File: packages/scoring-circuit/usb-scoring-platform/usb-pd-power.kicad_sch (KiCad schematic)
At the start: 33 parts, among them J12 PD service: GND SDA SCL, Q4 BSS138, Q5 BSS138, U19 LMR36510ADDAR, U20 TPS259470LRPWR, U5 STUSB4500QTR, U6 REC30K-2405SZ

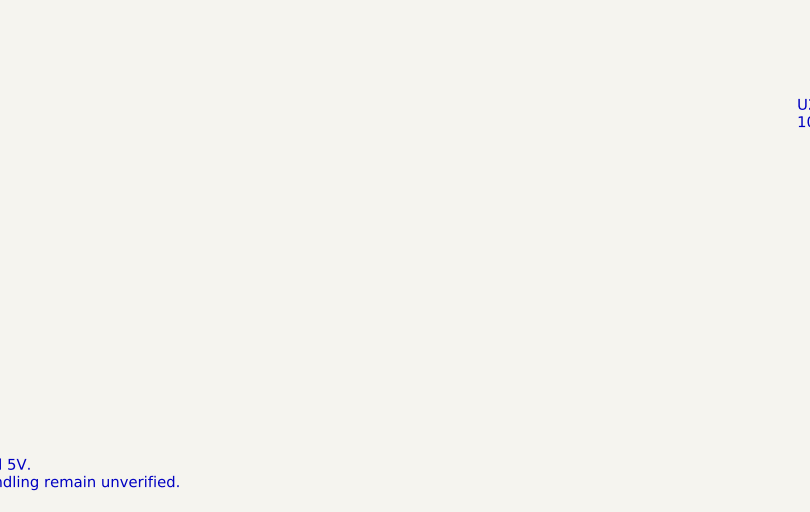
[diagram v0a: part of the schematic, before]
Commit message: feat(scoring-circuit): route protected isolated-power feed and eFuse support
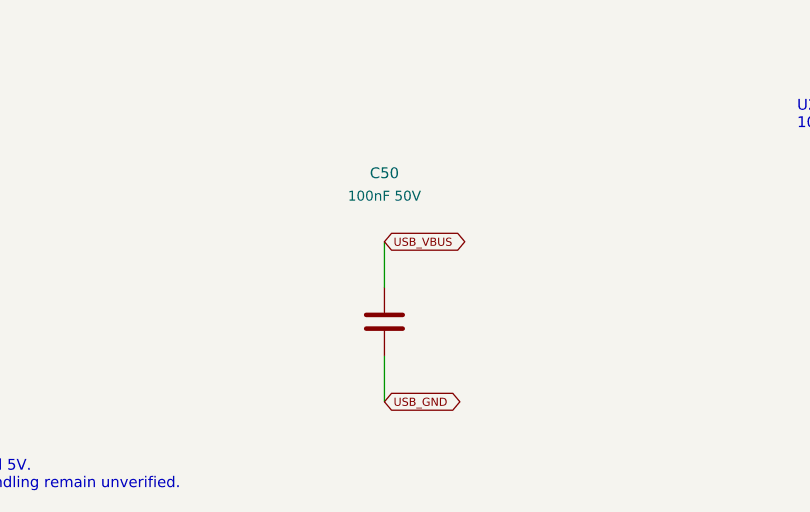
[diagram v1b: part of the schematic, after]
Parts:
- added C50: 100nF 50V, Capacitor_SMD:C_0805_2012Metric, symbol Device:C
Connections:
- net USB_GND: now also C50.2
- net USB_VBUS: now also C50.1
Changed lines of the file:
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@@
 (global_label "GND" (shape bidirectional) (at 519.43 373.38 0) (effects (font (size .9 .9)) (justify left)) (property "Intersheetrefs" "" (at 519.43 373.38 0) (effects (font (size 1 1)) (hide yes))))
 (symbol (lib_id "Device:C") (at 519.43 364.49 0) (unit 1) (in_bom yes) (on_board yes) (dnp no) (property "Reference" "C49" (at 519.43 347.98 0) (effects (font (size 1.2 1.2)))) (property "Value" "10uF 16V X7R" (at 519.43 350.52 0) (effects (font (size 1.1 1.1)))) (property "Footprint" "Capacitor_SMD:C_1206_3216Metric" (at 519.43 364.49 0) (effects (font (size 1 1)) (hide yes))) (property "Datasheet" "" (at 519.43 364.49 0) (effects (font (size 1 1)) (hide yes))) (instances (project "usb-scoring-platform" (path "/20cc8167-128c-446a-a106-f942323e143f/972b77fe-bd38-49a7-88fc-3c741d64cdb1" (reference "C49") (unit 1)))) (pin "1") (pin "2"))
+(wire (pts (xy 184.15 365.76) (xy 184.15 360.68)) (stroke (width 0) (type default)))
+(global_label "USB_VBUS" (shape bidirectional) (at 184.15 360.68 0) (effects (font (size .9 .9)) (justify left)) (property "Intersheetrefs" "" (at 184.15 360.68 0) (effects (font (size 1 1)) (hide yes))))
+(wire (pts (xy 184.15 373.38) (xy 184.15 378.46)) (stroke (width 0) (type default)))
+(global_label "USB_GND" (shape bidirectional) (at 184.15 378.46 0) (effects (font (size .9 .9)) (justify left)) (property "Intersheetrefs" "" (at 184.15 378.46 0) (effects (font (size 1 1)) (hide yes))))
+(symbol (lib_id "Device:C") (at 184.15 369.57 0) (unit 1) (in_bom yes) (on_board yes) (dnp no) (property "Reference" "C50" (at 184.15 353.06 0) (effects (font (size 1.2 1.2)))) (property "Value" "100nF 50V" (at 184.15 355.6 0) (effects (font (size 1.1 1.1)))) (property "Footprint" "Capacitor_SMD:C_0805_2012Metric" (at 184.15 369.57 0) (effects (font (size 1 1)) (hide yes))) (property "Datasheet" "" (at 184.15 369.57 0) (effects (font (size 1 1)) (hide yes))) (instances (project "usb-scoring-platform" (path "/20cc8167-128c-446a-a106-f942323e143f/972b77fe-bd38-49a7-88fc-3c741d64cdb1" (reference "C50") (unit 1)))) (pin "1") (pin "2"))
 (text "ONE USB-C: J1 VBUS / CC / USB_GND feed this primary-side sheet; D+/D- go through U18." (at 20 18 0) (effects (font (size 2 2)) (justify left top)))
 (text "No primary USB_GND connection to board GND. Only U18 and U6 cross the isolation boundary. Prototype: not for fabrication or fencer use." (at 20 27 0) (effects (font (size 1.2 1.2)) (justify left top)))

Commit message: feat(scoring-circuit): select exact prototype resistor parts
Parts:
- R88, R89: MPN (none) -> RC2512FK-071KL; Manufacturer (none) -> YAGEO
- R90, R92, R93: MPN (none) -> RC0603FR-07100KL; Manufacturer (none) -> YAGEO
- R91: MPN (none) -> RC0603FR-0724K9L; Manufacturer (none) -> YAGEO
- R94: MPN (none) -> RT0603BRD07140KL; Manufacturer (none) -> YAGEO
- R95, R97: MPN (none) -> RT0603BRD0710KL; Manufacturer (none) -> YAGEO
- R96: MPN (none) -> RT0603BRD07172KL; Manufacturer (none) -> YAGEO
- R98: MPN (none) -> RC0603FR-071K37L; Manufacturer (none) -> YAGEO

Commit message: feat(scoring-circuit): select bypass and timing capacitors
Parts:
- C42, C48: MPN (none) -> C1608X7R1H104K080AA; Manufacturer (none) -> TDK
- C45: MPN (none) -> C1608X7R1H103K080AA; Manufacturer (none) -> TDK
- C46, C50: MPN (none) -> C2012X7R2A104K125AA; Manufacturer (none) -> TDK

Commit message: feat(scoring-circuit): select local supply capacitors
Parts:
- C37, C38, C41: MPN (none) -> C1608X7R1H105K080AB; Manufacturer (none) -> TDK
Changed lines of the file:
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@@
 (wire (pts (xy 80.01 153.67) (xy 80.01 158.75)) (stroke (width 0) (type default)))
 (global_label "USB_GND" (shape bidirectional) (at 80.01 158.75 0) (effects (font (size .9 .9)) (justify left)) (property "Intersheetrefs" "" (at 80.01 158.75 0) (effects (font (size 1 1)) (hide yes))))
-(symbol (lib_id "Device:C") (at 80.01 149.86 0) (unit 1) (in_bom yes) (on_board yes) (dnp no) (property "Reference" "C37" (at 80.01 133.35000000000002 0) (effects (font (size 1.2 1.2)))) (property "Value" "1uF 10V" (at 80.01 135.89000000000001 0) (effects (font (size 1.1 1.1)))) (property "Footprint" "Capacitor_SMD:C_0603_1608Metric" (at 80.01 149.86 0) (effects (font (size 1 1)) (hide yes))) (property "Datasheet" "" (at 80.01 149.86 0) (effects (font (size 1 1)) (hide yes))) (instances (project "usb-scoring-platform" (path "/20cc8167-128c-446a-a106-f942323e143f/972b77fe-bd38-49a7-88fc-3c741d64cdb1" (reference "C37") (unit 1)))) (pin "1") (pin "2"))
+(symbol (lib_id "Device:C") (at 80.01 149.86 0) (unit 1) (in_bom yes) (on_board yes) (dnp no) (property "Reference" "C37" (at 80.01 133.35000000000002 0) (effects (font (size 1.2 1.2)))) (property "Value" "1uF 10V" (at 80.01 135.89000000000001 0) (effects (font (size 1.1 1.1)))) (property "Footprint" "Capacitor_SMD:C_0603_1608Metric" (at 80.01 149.86 0) (effects (font (size 1 1)) (hide yes))) (property "Manufacturer" "TDK" (at 80.01 149.86 0) (effects (font (size 1 1)) (hide yes))) (property "MPN" "C1608X7R1H105K080AB" (at 80.01 149.86 0) (effects (font (size 1 1)) (hide yes))) (property "Datasheet" "https://product.tdk.com/en/search/capacitor/ceramic/mlcc/info?part_no=C1608X7R1H105K080AB" (at 80.01 149.86 0) (effects (font (size 1 1)) (hide yes))) (instances (project "usb-scoring-platform" (path "/20cc8167-128c-446a-a106-f942323e143f/972b77fe-bd38-49a7-88fc-3c741d64cdb1" (reference "C37") (unit 1)))) (pin "1") (pin "2"))
 (wire (pts (xy 119.38 146.05) (xy 119.38 140.97)) (stroke (width 0) (type default)))
 (global_label "PD_VREG2V7" (shape bidirectional) (at 119.38 140.97 0) (effects (font (size .9 .9)) (justify left)) (property "Intersheetrefs" "" (at 119.38 140.97 0) (effects (font (size 1 1)) (hide yes))))
 (wire (pts (xy 119.38 153.67) (xy 119.38 158.75)) (stroke (width 0) (type default)))
 (global_label "USB_GND" (shape bidirectional) (at 119.38 158.75 0) (effects (font (size .9 .9)) (justify left)) (property "Intersheetrefs" "" (at 119.38 158.75 0) (effects (font (size 1 1)) (hide yes))))
-(symbol (lib_id "Device:C") (at 119.38 149.86 0) (unit 1) (in_bom yes) (on_board yes) (dnp no) (property "Reference" "C38" (at 119.38 133.35000000000002 0) (effects (font (size 1.2 1.2)))) (property "Value" "1uF 10V" (at 119.38 135.89000000000001 0) (effects (font (size 1.1 1.1)))) (property "Footprint" "Capacitor_SMD:C_0603_1608Metric" (at 119.38 149.86 0) (effects (font (size 1 1)) (hide yes))) (property "Datasheet" "" (at 119.38 149.86 0) (effects (font (size 1 1)) (hide yes))) (instances (project "usb-scoring-platform" (path "/20cc8167-128c-446a-a106-f942323e143f/972b77fe-bd38-49a7-88fc-3c741d64cdb1" (reference "C38") (unit 1)))) (pin "1") (pin "2"))
+(symbol (lib_id "Device:C") (at 119.38 149.86 0) (unit 1) (in_bom yes) (on_board yes) (dnp no) (property "Reference" "C38" (at 119.38 133.35000000000002 0) (effects (font (size 1.2 1.2)))) (property "Value" "1uF 10V" (at 119.38 135.89000000000001 0) (effects (font (size 1.1 1.1)))) (property "Footprint" "Capacitor_SMD:C_0603_1608Metric" (at 119.38 149.86 0) (effects (font (size 1 1)) (hide yes))) (property "Manufacturer" "TDK" (at 119.38 149.86 0) (effects (font (size 1 1)) (hide yes))) (property "MPN" "C1608X7R1H105K080AB" (at 119.38 149.86 0) (effects (font (size 1 1)) (hide yes))) (property "Datasheet" "https://product.tdk.com/en/search/capacitor/ceramic/mlcc/info?part_no=C1608X7R1H105K080AB" (at 119.38 149.86 0) (effects (font (size 1 1)) (hide yes))) (instances (project "usb-scoring-platform" (path "/20cc8167-128c-446a-a106-f942323e143f/972b77fe-bd38-49a7-88fc-3c741d64cdb1" (reference "C38") (unit 1)))) (pin "1") (pin "2"))
 (wire (pts (xy 160.02 146.05) (xy 160.02 140.97)) (stroke (width 0) (type default)))
 (global_label "USB_VBUS" (shape bidirectional) (at 160.02 140.97 0) (effects (font (size .9 .9)) (justify left)) (property "Intersheetrefs" "" (at 160.02 140.97 0) (effects (font (size 1 1)) (hide yes))))
@@
 (wire (pts (xy 325.12 153.67) (xy 325.12 158.75)) (stroke (width 0) (type default)))
 (global_label "USB_GND" (shape bidirectional) (at 325.12 158.75 0) (effects (font (size .9 .9)) (justify left)) (property "Intersheetrefs" "" (at 325.12 158.75 0) (effects (font (size 1 1)) (hide yes))))
-(symbol (lib_id "Device:C") (at 325.12 149.86 0) (unit 1) (in_bom yes) (on_board yes) (dnp no) (property "Reference" "C41" (at 325.12 133.35000000000002 0) (effects (font (size 1.2 1.2)))) (property "Value" "1uF 10V" (at 325.12 135.89000000000001 0) (effects (font (size 1.1 1.1)))) (property "Footprint" "Capacitor_SMD:C_0603_1608Metric" (at 325.12 149.86 0) (effects (font (size 1 1)) (hide yes))) (property "Datasheet" "" (at 325.12 149.86 0) (effects (font (size 1 1)) (hide yes))) (instances (project "usb-scoring-platform" (path "/20cc8167-128c-446a-a106-f942323e143f/972b77fe-bd38-49a7-88fc-3c741d64cdb1" (reference "C41") (unit 1)))) (pin "1") (pin "2"))
+(symbol (lib_id "Device:C") (at 325.12 149.86 0) (unit 1) (in_bom yes) (on_board yes) (dnp no) (property "Reference" "C41" (at 325.12 133.35000000000002 0) (effects (font (size 1.2 1.2)))) (property "Value" "1uF 10V" (at 325.12 135.89000000000001 0) (effects (font (size 1.1 1.1)))) (property "Footprint" "Capacitor_SMD:C_0603_1608Metric" (at 325.12 149.86 0) (effects (font (size 1 1)) (hide yes))) (property "Manufacturer" "TDK" (at 325.12 149.86 0) (effects (font (size 1 1)) (hide yes))) (property "MPN" "C1608X7R1H105K080AB" (at 325.12 149.86 0) (effects (font (size 1 1)) (hide yes))) (property "Datasheet" "https://product.tdk.com/en/search/capacitor/ceramic/mlcc/info?part_no=C1608X7R1H105K080AB" (at 325.12 149.86 0) (effects (font (size 1 1)) (hide yes))) (instances (project "usb-scoring-platform" (path "/20cc8167-128c-446a-a106-f942323e143f/972b77fe-bd38-49a7-88fc-3c741d64cdb1" (reference "C41") (unit 1)))) (pin "1") (pin "2"))
 (wire (pts (xy 364.49 146.05) (xy 364.49 140.97)) (stroke (width 0) (type default)))
 (global_label "USB_BUCK_BOOT" (shape bidirectional) (at 364.49 140.97 0) (effects (font (size .9 .9)) (justify left)) (property "Intersheetrefs" "" (at 364.49 140.97 0) (effects (font (size 1 1)) (hide yes))))

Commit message: feat(scoring-circuit): select USB input capacitors
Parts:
- C36: MPN (none) -> C2012X7R1H105K125AB; Manufacturer (none) -> TDK
- C39: MPN (none) -> C3216X7R1H225K160AB; Manufacturer (none) -> TDK
- C40: MPN (none) -> C2012X7R1H224K125AA; Manufacturer (none) -> TDK
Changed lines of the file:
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@@
 (wire (pts (xy 39.37 153.67) (xy 39.37 158.75)) (stroke (width 0) (type default)))
 (global_label "USB_GND" (shape bidirectional) (at 39.37 158.75 0) (effects (font (size .9 .9)) (justify left)) (property "Intersheetrefs" "" (at 39.37 158.75 0) (effects (font (size 1 1)) (hide yes))))
-(symbol (lib_id "Device:C") (at 39.37 149.86 0) (unit 1) (in_bom yes) (on_board yes) (dnp no) (property "Reference" "C36" (at 39.37 133.35000000000002 0) (effects (font (size 1.2 1.2)))) (property "Value" "1uF 50V" (at 39.37 135.89000000000001 0) (effects (font (size 1.1 1.1)))) (property "Footprint" "Capacitor_SMD:C_0805_2012Metric" (at 39.37 149.86 0) (effects (font (size 1 1)) (hide yes))) (property "Datasheet" "" (at 39.37 149.86 0) (effects (font (size 1 1)) (hide yes))) (instances (project "usb-scoring-platform" (path "/20cc8167-128c-446a-a106-f942323e143f/972b77fe-bd38-49a7-88fc-3c741d64cdb1" (reference "C36") (unit 1)))) (pin "1") (pin "2"))
+(symbol (lib_id "Device:C") (at 39.37 149.86 0) (unit 1) (in_bom yes) (on_board yes) (dnp no) (property "Reference" "C36" (at 39.37 133.35000000000002 0) (effects (font (size 1.2 1.2)))) (property "Value" "1uF 50V" (at 39.37 135.89000000000001 0) (effects (font (size 1.1 1.1)))) (property "Footprint" "Capacitor_SMD:C_0805_2012Metric" (at 39.37 149.86 0) (effects (font (size 1 1)) (hide yes))) (property "Datasheet" "https://product.tdk.com/en/search/capacitor/ceramic/mlcc/info?part_no=C2012X7R1H105K125AB" (at 39.37 149.86 0) (effects (font (size 1 1)) (hide yes))) (property "Manufacturer" "TDK" (at 0 0 0) (effects (font (size 1 1)) (hide yes))) (property "MPN" "C2012X7R1H105K125AB" (at 0 0 0) (effects (font (size 1 1)) (hide yes))) (instances (project "usb-scoring-platform" (path "/20cc8167-128c-446a-a106-f942323e143f/972b77fe-bd38-49a7-88fc-3c741d64cdb1" (reference "C36") (unit 1)))) (pin "1") (pin "2"))
 (wire (pts (xy 80.01 146.05) (xy 80.01 140.97)) (stroke (width 0) (type default)))
 (global_label "PD_VREG1V2" (shape bidirectional) (at 80.01 140.97 0) (effects (font (size .9 .9)) (justify left)) (property "Intersheetrefs" "" (at 80.01 140.97 0) (effects (font (size 1 1)) (hide yes))))
@@
 (wire (pts (xy 245.11 153.67) (xy 245.11 158.75)) (stroke (width 0) (type default)))
 (global_label "USB_GND" (shape bidirectional) (at 245.11 158.75 0) (effects (font (size .9 .9)) (justify left)) (property "Intersheetrefs" "" (at 245.11 158.75 0) (effects (font (size 1 1)) (hide yes))))
-(symbol (lib_id "Device:C") (at 245.11 149.86 0) (unit 1) (in_bom yes) (on_board yes) (dnp no) (property "Reference" "C39" (at 245.11 133.35000000000002 0) (effects (font (size 1.2 1.2)))) (property "Value" "2.2uF 50V" (at 245.11 135.89000000000001 0) (effects (font (size 1.1 1.1)))) (property "Footprint" "Capacitor_SMD:C_1206_3216Metric" (at 245.11 149.86 0) (effects (font (size 1 1)) (hide yes))) (property "Datasheet" "" (at 245.11 149.86 0) (effects (font (size 1 1)) (hide yes))) (instances (project "usb-scoring-platform" (path "/20cc8167-128c-446a-a106-f942323e143f/972b77fe-bd38-49a7-88fc-3c741d64cdb1" (reference "C39") (unit 1)))) (pin "1") (pin "2"))
+(symbol (lib_id "Device:C") (at 245.11 149.86 0) (unit 1) (in_bom yes) (on_board yes) (dnp no) (property "Reference" "C39" (at 245.11 133.35000000000002 0) (effects (font (size 1.2 1.2)))) (property "Value" "2.2uF 50V" (at 245.11 135.89000000000001 0) (effects (font (size 1.1 1.1)))) (property "Footprint" "Capacitor_SMD:C_1206_3216Metric" (at 245.11 149.86 0) (effects (font (size 1 1)) (hide yes))) (property "Datasheet" "https://product.tdk.com/en/search/capacitor/ceramic/mlcc/info?part_no=C3216X7R1H225K160AB" (at 245.11 149.86 0) (effects (font (size 1 1)) (hide yes))) (property "Manufacturer" "TDK" (at 0 0 0) (effects (font (size 1 1)) (hide yes))) (property "MPN" "C3216X7R1H225K160AB" (at 0 0 0) (effects (font (size 1 1)) (hide yes))) (instances (project "usb-scoring-platform" (path "/20cc8167-128c-446a-a106-f942323e143f/972b77fe-bd38-49a7-88fc-3c741d64cdb1" (reference "C39") (unit 1)))) (pin "1") (pin "2"))
 (wire (pts (xy 284.48 146.05) (xy 284.48 140.97)) (stroke (width 0) (type default)))
 (global_label "USB_VBUS" (shape bidirectional) (at 284.48 140.97 0) (effects (font (size .9 .9)) (justify left)) (property "Intersheetrefs" "" (at 284.48 140.97 0) (effects (font (size 1 1)) (hide yes))))
 (wire (pts (xy 284.48 153.67) (xy 284.48 158.75)) (stroke (width 0) (type default)))
 (global_label "USB_GND" (shape bidirectional) (at 284.48 158.75 0) (effects (font (size .9 .9)) (justify left)) (property "Intersheetrefs" "" (at 284.48 158.75 0) (effects (font (size 1 1)) (hide yes))))
-(symbol (lib_id "Device:C") (at 284.48 149.86 0) (unit 1) (in_bom yes) (on_board yes) (dnp no) (property "Reference" "C40" (at 284.48 133.35000000000002 0) (effects (font (size 1.2 1.2)))) (property "Value" "220nF 50V" (at 284.48 135.89000000000001 0) (effects (font (size 1.1 1.1)))) (property "Footprint" "Capacitor_SMD:C_0805_2012Metric" (at 284.48 149.86 0) (effects (font (size 1 1)) (hide yes))) (property "Datasheet" "" (at 284.48 149.86 0) (effects (font (size 1 1)) (hide yes))) (instances (project "usb-scoring-platform" (path "/20cc8167-128c-446a-a106-f942323e143f/972b77fe-bd38-49a7-88fc-3c741d64cdb1" (reference "C40") (unit 1)))) (pin "1") (pin "2"))
+(symbol (lib_id "Device:C") (at 284.48 149.86 0) (unit 1) (in_bom yes) (on_board yes) (dnp no) (property "Reference" "C40" (at 284.48 133.35000000000002 0) (effects (font (size 1.2 1.2)))) (property "Value" "220nF 50V" (at 284.48 135.89000000000001 0) (effects (font (size 1.1 1.1)))) (property "Footprint" "Capacitor_SMD:C_0805_2012Metric" (at 284.48 149.86 0) (effects (font (size 1 1)) (hide yes))) (property "Datasheet" "https://product.tdk.com/en/search/capacitor/ceramic/mlcc/info?part_no=C2012X7R1H224K125AA" (at 284.48 149.86 0) (effects (font (size 1 1)) (hide yes))) (property "Manufacturer" "TDK" (at 0 0 0) (effects (font (size 1 1)) (hide yes))) (property "MPN" "C2012X7R1H224K125AA" (at 0 0 0) (effects (font (size 1 1)) (hide yes))) (instances (project "usb-scoring-platform" (path "/20cc8167-128c-446a-a106-f942323e143f/972b77fe-bd38-49a7-88fc-3c741d64cdb1" (reference "C40") (unit 1)))) (pin "1") (pin "2"))
 (wire (pts (xy 325.12 146.05) (xy 325.12 140.97)) (stroke (width 0) (type default)))
 (global_label "USB_BUCK_VCC" (shape bidirectional) (at 325.12 140.97 0) (effects (font (size .9 .9)) (justify left)) (property "Intersheetrefs" "" (at 325.12 140.97 0) (effects (font (size 1 1)) (hide yes))))
